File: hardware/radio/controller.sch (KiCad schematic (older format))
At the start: 12 parts, among them IC301 ATMEGA328-A, Q301 BSH105, X301 8MHz

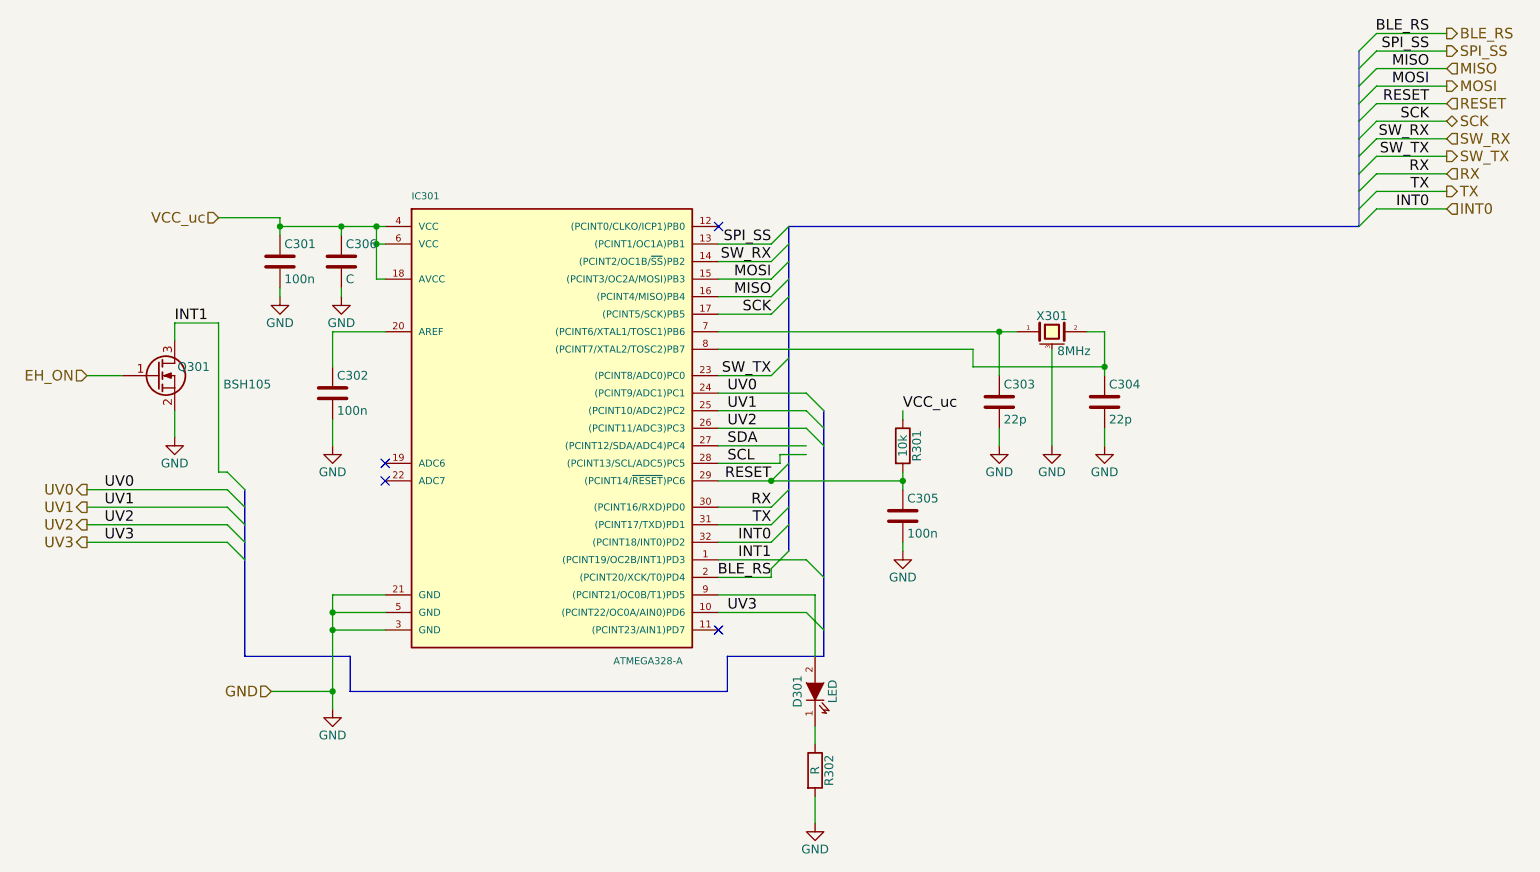
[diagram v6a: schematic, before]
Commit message: Compress schematics for printouts
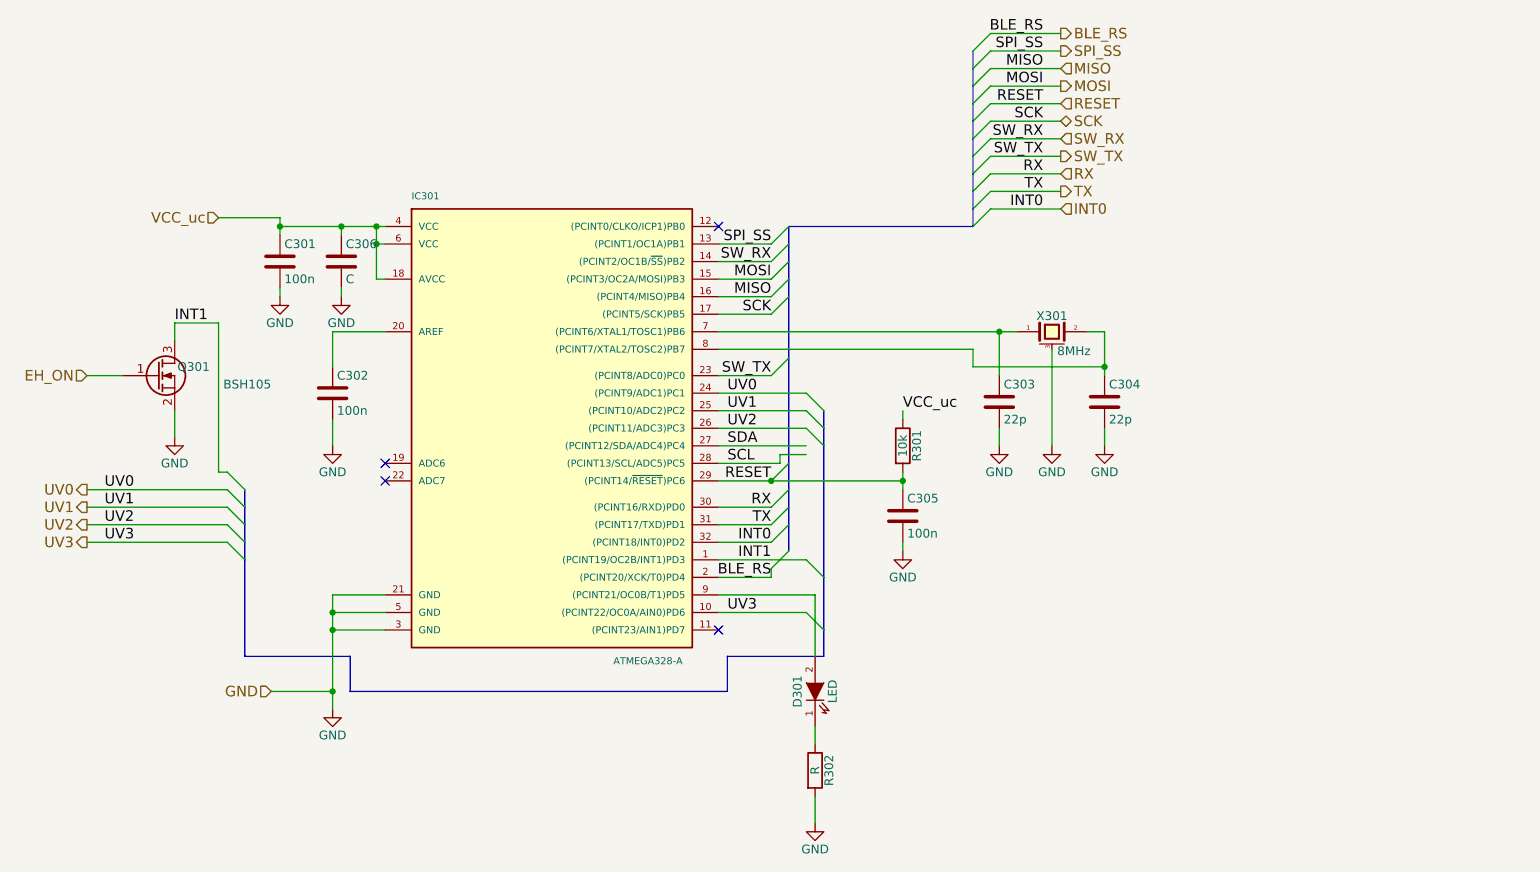
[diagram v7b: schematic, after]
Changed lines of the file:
@@
 $EndComp
 Entry Wire Line
-	9050 1300 9150 1200
-Entry Wire Line
-	9050 1400 9150 1300
-Entry Wire Line
-	9050 1500 9150 1400
-Entry Wire Line
-	9050 1600 9150 1500
-Entry Wire Line
-	9050 1700 9150 1600
-Entry Wire Line
-	9050 1800 9150 1700
-Entry Wire Line
-	9050 1900 9150 1800
-Entry Wire Line
-	9050 1200 9150 1100
-Entry Wire Line
-	9050 1100 9150 1000
+	6850 1300 6950 1200
+Entry Wire Line
+	6850 1400 6950 1300
+Entry Wire Line
+	6850 1500 6950 1400
+Entry Wire Line
+	6850 1600 6950 1500
+Entry Wire Line
+	6850 1700 6950 1600
+Entry Wire Line
+	6850 1800 6950 1700
+Entry Wire Line
+	6850 1900 6950 1800
+Entry Wire Line
+	6850 1200 6950 1100
+Entry Wire Line
+	6850 1100 6950 1000
 Entry Wire Line
 	5700 2200 5800 2100
@@
 Text Label 5700 3900 2    60   ~ 0
 INT1
-Text Label 9450 1000 2    60   ~ 0
+Text Label 7250 1000 2    60   ~ 0
 SPI_SS
-Text Label 9450 1100 2    60   ~ 0
+Text Label 7250 1100 2    60   ~ 0
 MISO
-Text Label 9450 1200 2    60   ~ 0
+Text Label 7250 1200 2    60   ~ 0
 MOSI
-Text Label 9450 1300 2    60   ~ 0
+Text Label 7250 1300 2    60   ~ 0
 RESET
-Text Label 9450 1400 2    60   ~ 0
+Text Label 7250 1400 2    60   ~ 0
 SCK
-Text Label 9450 1500 2    60   ~ 0
+Text Label 7250 1500 2    60   ~ 0
 SW_RX
-Text Label 9450 1600 2    60   ~ 0
+Text Label 7250 1600 2    60   ~ 0
 SW_TX
-Text Label 9450 1700 2    60   ~ 0
+Text Label 7250 1700 2    60   ~ 0
 RX
-Text Label 9450 1800 2    60   ~ 0
+Text Label 7250 1800 2    60   ~ 0
 TX
 Entry Wire Line
-	9050 2000 9150 1900
-Text Label 9450 1900 2    60   ~ 0
+	6850 2000 6950 1900
+Text Label 7250 1900 2    60   ~ 0
 INT0
-Text HLabel 9550 1000 2    60   Output ~ 0
+Text HLabel 7350 1000 2    60   Output ~ 0
 SPI_SS
-Text HLabel 9550 1100 2    60   Input ~ 0
+Text HLabel 7350 1100 2    60   Input ~ 0
 MISO
-Text HLabel 9550 1200 2    60   Output ~ 0
+Text HLabel 7350 1200 2    60   Output ~ 0
 MOSI
-Text HLabel 9550 1300 2    60   Input ~ 0
+Text HLabel 7350 1300 2    60   Input ~ 0
 RESET
-Text HLabel 9550 1400 2    60   BiDi ~ 0
+Text HLabel 7350 1400 2    60   BiDi ~ 0
 SCK
-Text HLabel 9550 1500 2    60   Input ~ 0
+Text HLabel 7350 1500 2    60   Input ~ 0
 SW_RX
-Text HLabel 9550 1600 2    60   Output ~ 0
+Text HLabel 7350 1600 2    60   Output ~ 0
 SW_TX
-Text HLabel 9550 1700 2    60   Input ~ 0
+Text HLabel 7350 1700 2    60   Input ~ 0
 RX
-Text HLabel 9550 1800 2    60   Output ~ 0
+Text HLabel 7350 1800 2    60   Output ~ 0
 TX
-Text HLabel 9550 1900 2    60   Input ~ 0
+Text HLabel 7350 1900 2    60   Input ~ 0
 INT0
 Text HLabel 2850 4650 0    60   Input ~ 0
@@
 	2600 3800 2700 3900
 Wire Wire Line
-	5400 2600 7100 2600
+	5400 2600 7000 2600
+Wire Wire Line
+	7000 2600 7100 2600
 Wire Wire Line
 	5400 2700 6850 2700
@@
 	6850 2800 7600 2800
 Wire Wire Line
-	7600 2600 7600 2850
+	7600 2600 7600 2800
+Wire Wire Line
+	7600 2800 7600 2850
 Wire Wire Line
 	7600 2600 7500 2600
@@
 	7600 3150 7600 3250
 Wire Bus Line
-	5800 2000 5800 3850
-Wire Bus Line
-	9050 2000 5800 2000
+	5800 2000 5800 2100
+Wire Bus Line
+	5800 2100 5800 2200
+Wire Bus Line
+	5800 2200 5800 2300
+Wire Bus Line
+	5800 2300 5800 2400
+Wire Bus Line
+	5800 2400 5800 2750
+Wire Bus Line
+	5800 2750 5800 3500
+Wire Bus Line
+	5800 3500 5800 3600
+Wire Bus Line
+	5800 3600 5800 3700
+Wire Bus Line
+	5800 3700 5800 3850
+Wire Bus Line
+	6850 2000 5800 2000
 Wire Wire Line
 	5700 2500 5400 2500
@@
 	5400 2100 5700 2100
 Wire Wire Line
-	5400 3450 6450 3450
-Wire Wire Line
-	6450 3400 6450 3500
+	5400 3450 5700 3450
+Wire Wire Line
+	5700 3450 6450 3450
+Wire Wire Line
+	6450 3400 6450 3450
+Wire Wire Line
+	6450 3450 6450 3500
 Wire Wire Line
 	6450 3050 6450 3100
@@
 	3500 4200 3200 4200
 Wire Wire Line
-	3200 4100 3200 4750
+	3200 4100 3200 4200
+Wire Wire Line
+	3200 4200 3200 4300
+Wire Wire Line
+	3200 4300 3200 4650
+Wire Wire Line
+	3200 4650 3200 4750
 Wire Wire Line
 	3500 4300 3200 4300
@@
 	3450 2300 3500 2300
 Wire Wire Line
-	3450 2000 3450 2300
-Wire Wire Line
-	2900 2000 3500 2000
+	3450 2000 3450 2100
+Wire Wire Line
+	3450 2100 3450 2300
+Wire Wire Line
+	2900 2000 3250 2000
+Wire Wire Line
+	3250 2000 3450 2000
+Wire Wire Line
+	3450 2000 3500 2000
 Connection ~ 3450 2000
 Wire Wire Line
@@
 	2900 2350 2900 2400
 Wire Bus Line
-	9050 1000 9050 2000
+	6850 1000 6850 1100
+Wire Bus Line
+	6850 1100 6850 1200
+Wire Bus Line
+	6850 1200 6850 1300
+Wire Bus Line
+	6850 1300 6850 1400
+Wire Bus Line
+	6850 1400 6850 1500
+Wire Bus Line
+	6850 1500 6850 1600
+Wire Bus Line
+	6850 1600 6850 1700
+Wire Bus Line
+	6850 1700 6850 1800
+Wire Bus Line
+	6850 1800 6850 1900
+Wire Bus Line
+	6850 1900 6850 2000
 Wire Wire Line
 	5400 3800 5700 3800
@@
 	5400 3900 5900 3900
 Wire Wire Line
-	9150 1000 9550 1000
-Wire Wire Line
-	9150 1100 9550 1100
-Wire Wire Line
-	9150 1200 9550 1200
-Wire Wire Line
-	9150 1300 9550 1300
-Wire Wire Line
-	9150 1400 9550 1400
-Wire Wire Line
-	9150 1500 9550 1500
-Wire Wire Line
-	9150 1600 9550 1600
-Wire Wire Line
-	9150 1700 9550 1700
-Wire Wire Line
-	9550 1800 9150 1800
-Wire Wire Line
-	9150 1900 9550 1900
+	6950 1000 7350 1000
+Wire Wire Line
+	6950 1100 7350 1100
+Wire Wire Line
+	6950 1200 7350 1200
+Wire Wire Line
+	6950 1300 7350 1300
+Wire Wire Line
+	6950 1400 7350 1400
+Wire Wire Line
+	6950 1500 7350 1500
+Wire Wire Line
+	6950 1600 7350 1600
+Wire Wire Line
+	6950 1700 7350 1700
+Wire Wire Line
+	7350 1800 6950 1800
+Wire Wire Line
+	6950 1900 7350 1900
 Wire Wire Line
 	2900 1950 2550 1950
@@
 	5900 4200 5400 4200
 Wire Bus Line
-	6000 3050 6000 4450
+	6000 3050 6000 3150
+Wire Bus Line
+	6000 3150 6000 3250
+Wire Bus Line
+	6000 3250 6000 4000
+Wire Bus Line
+	6000 4000 6000 4300
+Wire Bus Line
+	6000 4300 6000 4450
 Wire Bus Line
 	6000 4450 5450 4450
@@
 	3300 4450 2700 4450
 Wire Bus Line
-	2700 4450 2700 3500
+	2700 4450 2700 3900
+Wire Bus Line
+	2700 3900 2700 3800
+Wire Bus Line
+	2700 3800 2700 3700
+Wire Bus Line
+	2700 3700 2700 3600
+Wire Bus Line
+	2700 3600 2700 3500
 Wire Wire Line
 	2300 3050 2300 3200
@@
 BLE_RS
 Entry Wire Line
-	9050 1000 9150 900
-Wire Wire Line
-	9150 900  9550 900
-Text HLabel 9550 900  2    60   Output ~ 0
+	6850 1000 6950 900
+Wire Wire Line
+	6950 900  7350 900
+Text HLabel 7350 900  2    60   Output ~ 0
 BLE_RS
-Text Label 9450 900  2    60   ~ 0
+Text Label 7250 900  2    60   ~ 0
 BLE_RS
 Text Label 2300 2550 0    60   ~ 0
@@
 $EndComp
 Wire Wire Line
-	2900 1950 2900 2050
+	2900 1950 2900 2000
+Wire Wire Line
+	2900 2000 2900 2050
 Text Label 6450 3050 0    60   ~ 0
 VCC_uc

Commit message: Compress schematics for screenshots
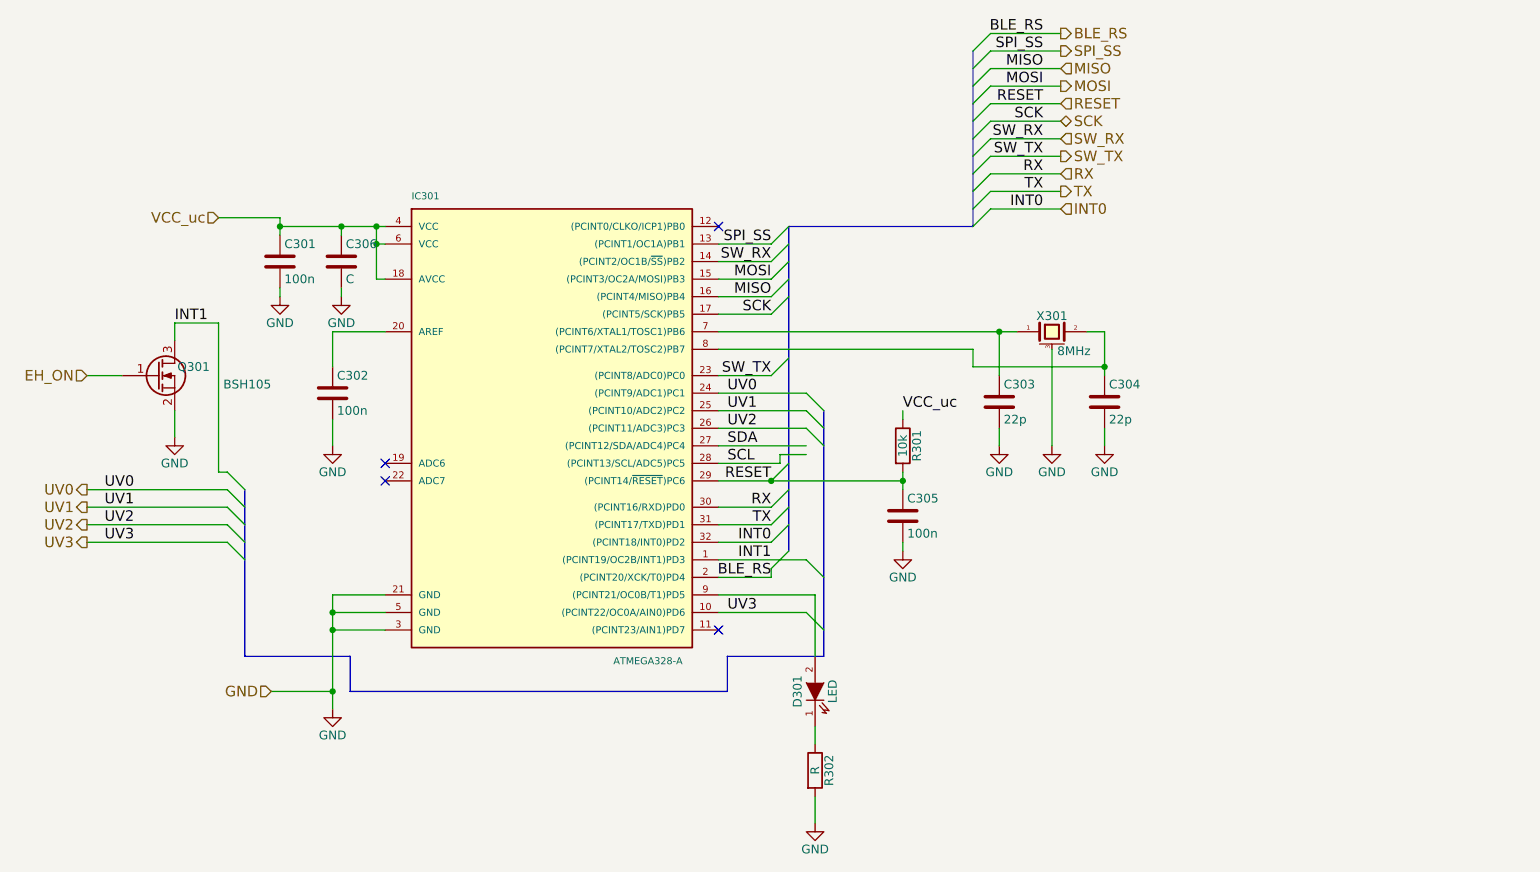
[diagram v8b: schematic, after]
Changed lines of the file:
@@
 	2600 3800 2700 3900
 Wire Wire Line
-	5400 2600 7000 2600
-Wire Wire Line
-	7000 2600 7100 2600
+	5400 2600 7100 2600
 Wire Wire Line
 	5400 2700 6850 2700
@@
 	6850 2800 7600 2800
 Wire Wire Line
-	7600 2600 7600 2800
-Wire Wire Line
-	7600 2800 7600 2850
+	7600 2600 7600 2850
 Wire Wire Line
 	7600 2600 7500 2600
@@
 	7600 3150 7600 3250
 Wire Bus Line
-	5800 2000 5800 2100
-Wire Bus Line
-	5800 2100 5800 2200
-Wire Bus Line
-	5800 2200 5800 2300
-Wire Bus Line
-	5800 2300 5800 2400
-Wire Bus Line
-	5800 2400 5800 2750
-Wire Bus Line
-	5800 2750 5800 3500
-Wire Bus Line
-	5800 3500 5800 3600
-Wire Bus Line
-	5800 3600 5800 3700
-Wire Bus Line
-	5800 3700 5800 3850
+	5800 2000 5800 3850
 Wire Bus Line
 	6850 2000 5800 2000
@@
 	5400 2100 5700 2100
 Wire Wire Line
-	5400 3450 5700 3450
-Wire Wire Line
-	5700 3450 6450 3450
-Wire Wire Line
-	6450 3400 6450 3450
-Wire Wire Line
-	6450 3450 6450 3500
+	5400 3450 6450 3450
+Wire Wire Line
+	6450 3400 6450 3500
 Wire Wire Line
 	6450 3050 6450 3100
@@
 	3500 4200 3200 4200
 Wire Wire Line
-	3200 4100 3200 4200
-Wire Wire Line
-	3200 4200 3200 4300
-Wire Wire Line
-	3200 4300 3200 4650
-Wire Wire Line
-	3200 4650 3200 4750
+	3200 4100 3200 4750
 Wire Wire Line
 	3500 4300 3200 4300
@@
 	3450 2300 3500 2300
 Wire Wire Line
-	3450 2000 3450 2100
-Wire Wire Line
-	3450 2100 3450 2300
-Wire Wire Line
-	2900 2000 3250 2000
-Wire Wire Line
-	3250 2000 3450 2000
-Wire Wire Line
-	3450 2000 3500 2000
+	3450 2000 3450 2300
+Wire Wire Line
+	2900 2000 3500 2000
 Connection ~ 3450 2000
 Wire Wire Line
@@
 	2900 2350 2900 2400
 Wire Bus Line
-	6850 1000 6850 1100
-Wire Bus Line
-	6850 1100 6850 1200
-Wire Bus Line
-	6850 1200 6850 1300
-Wire Bus Line
-	6850 1300 6850 1400
-Wire Bus Line
-	6850 1400 6850 1500
-Wire Bus Line
-	6850 1500 6850 1600
-Wire Bus Line
-	6850 1600 6850 1700
-Wire Bus Line
-	6850 1700 6850 1800
-Wire Bus Line
-	6850 1800 6850 1900
-Wire Bus Line
-	6850 1900 6850 2000
+	6850 1000 6850 2000
 Wire Wire Line
 	5400 3800 5700 3800
@@
 	5900 4200 5400 4200
 Wire Bus Line
-	6000 3050 6000 3150
-Wire Bus Line
-	6000 3150 6000 3250
-Wire Bus Line
-	6000 3250 6000 4000
-Wire Bus Line
-	6000 4000 6000 4300
-Wire Bus Line
-	6000 4300 6000 4450
+	6000 3050 6000 4450
 Wire Bus Line
 	6000 4450 5450 4450
@@
 	3300 4650 3300 4450
 Wire Bus Line
-	3300 4450 2700 4450
-Wire Bus Line
-	2700 4450 2700 3900
-Wire Bus Line
-	2700 3900 2700 3800
-Wire Bus Line
-	2700 3800 2700 3700
-Wire Bus Line
-	2700 3700 2700 3600
-Wire Bus Line
-	2700 3600 2700 3500
+	2700 4450 3300 4450
+Wire Bus Line
+	2700 3500 2700 4450
 Wire Wire Line
 	2300 3050 2300 3200
@@
 $EndComp
 Wire Wire Line
-	2900 1950 2900 2000
-Wire Wire Line
-	2900 2000 2900 2050
+	2900 1950 2900 2050
 Text Label 6450 3050 0    60   ~ 0
 VCC_uc
